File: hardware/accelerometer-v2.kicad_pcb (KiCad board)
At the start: 2 copper layers, 20 x 25 mm, 25 parts, among them P1 CON-SENSOR, P2 Debug, P3 Boot, U1 XMC1100, U2 KX122-1037, U3 DRILL, U4 DRILL, U5 DRILL, U6 DRILL

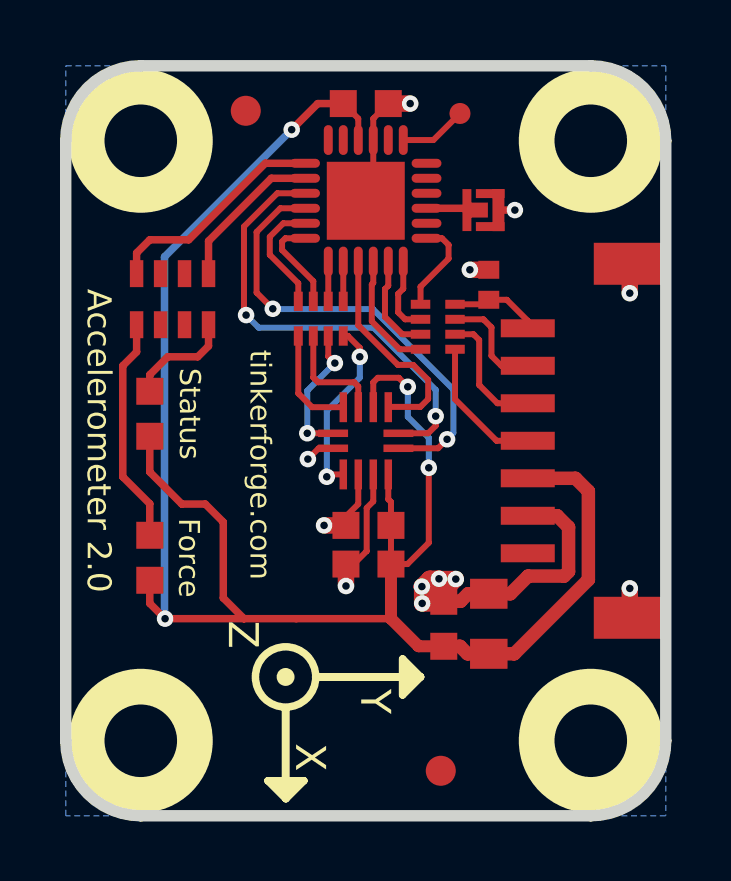
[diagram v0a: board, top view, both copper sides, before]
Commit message: fix footprint numbering and routing
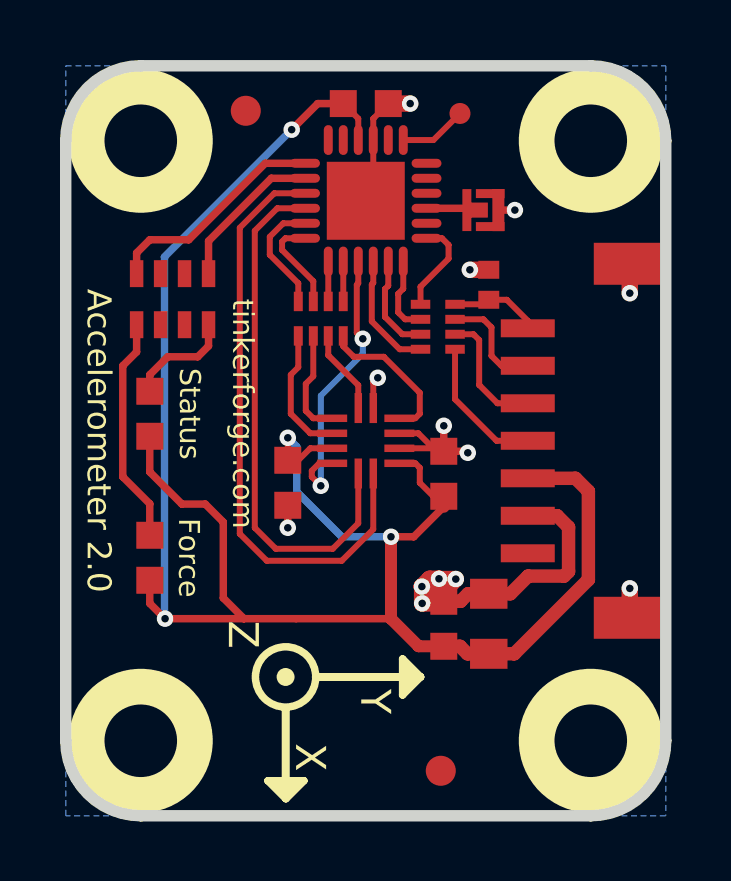
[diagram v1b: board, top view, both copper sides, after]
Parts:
- moved C5 3.82 mm to (128.9, 101.6), turned to 270 degrees
- moved C6 3.04 mm to (134.1, 101.3), turned to 90 degrees
- turned U2 to 0 degrees
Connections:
- P1 pad 1: Net-(P1-Pad1) -> (no net)
- RP2 pad 7: M-MOSI -> M-MISO
- RP2 pad 8: M-MISO -> M-MOSI
- RP3 pad 2: Net-(RP3-Pad2) -> (no net)
- RP3 pad 3: Net-(RP3-Pad3) -> (no net)
- RP3 pad 6: Net-(RP3-Pad6) -> (no net)
- RP3 pad 7: Net-(RP3-Pad7) -> (no net)
- U1 pad 11: Net-(U1-Pad11) -> (no net)
- U1 pad 12: Net-(U1-Pad12) -> (no net)
- U1 pad 15: INT1 -> INT2
- U1 pad 16: INT2 -> INT1
- U1 pad 17: M-MISO -> M-MOSI
- U1 pad 18: M-MOSI -> M-MISO
- U1 pad 2: Net-(U1-Pad2) -> (no net)
- U1 pad 4: Net-(U1-Pad4) -> (no net)
- U1 pad 5: Net-(U1-Pad5) -> (no net)
- U1 pad 6: Net-(U1-Pad6) -> (no net)
- U1 pad 8: Net-(U1-Pad8) -> (no net)
- U2 pad 1: Net-(RP2-Pad1) -> Net-(RP2-Pad2)
- U2 pad 2: Net-(RP2-Pad2) -> Net-(RP2-Pad1)
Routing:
- net INT2: track 15.4 -> 20.0 mm, vias 2 -> 0
- net TRIG: track 7.29 -> 9.57 mm, vias 0 -> 2
- net INT1: track 15.4 -> 17.6 mm, vias 2 -> 0
- net VCC: track 65.7 -> 67.7 mm
- net Net-(RP2-Pad3): track 4.58 -> 2.82 mm, vias 2 -> 0
- net GND: track 35.3 -> 34.2 mm, vias 12 -> 13
- net Net-(RP2-Pad4): track 6.05 -> 4.98 mm, vias 2 -> 0
- net Net-(RP2-Pad1): track 3.61 -> 4.35 mm
- net M-MOSI: track 3.24 -> 3.91 mm
- net M-MISO: track 3.91 -> 3.24 mm

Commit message: change processor xmc1100 -> xmc1302
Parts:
- U1: value XMC1100 -> XMC1302
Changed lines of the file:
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@@
-(kicad_pcb (version 20171130) (host pcbnew 5.0.1-33cea8e~67~ubuntu18.04.1)
+(kicad_pcb (version 20171130) (host pcbnew 5.0.1-33cea8e~68~ubuntu18.04.1)
   (general
     (thickness 1.6002)
@@
       (effects (font (size 0.3 0.3) (thickness 0.075)))
     )
-    (fp_text value XMC1100 (at 0 0.8 180) (layer F.Fab)
+    (fp_text value XMC1302 (at 0 0.8 180) (layer F.Fab)
       (effects (font (size 0.3 0.3) (thickness 0.075)))
     )
@@
   (segment (start 131.1 97.4) (end 132.1 97.4) (width 0.2) (layer Vorderseite) (net 17))
   (segment (start 130.7493 97.0493) (end 131.1 97.4) (width 0.2) (layer Vorderseite) (net 17))
+  (segment (start 129.475 92.95) (end 128.75 92.95) (width 0.2) (layer Vorderseite) (net 18))
+  (segment (start 129.2507 94.9507) (end 129.2507 95.555) (width 0.2) (layer Vorderseite) (net 18))
+  (segment (start 128.3 94) (end 129.2507 94.9507) (width 0.2) (layer Vorderseite) (net 18))
+  (segment (start 128.3 93.4) (end 128.3 94) (width 0.2) (layer Vorderseite) (net 18))
+  (segment (start 128.75 92.95) (end 128.3 93.4) (width 0.2) (layer Vorderseite) (net 18))
+  (segment (start 130.25 94.225) (end 130.25 95.55392) (width 0.2) (layer Vorderseite) (net 19))
+  (segment (start 130.25 95.55392) (end 130.24892 95.555) (width 0.2) (layer Vorderseite) (net 19))
+  (segment (start 130.75 94.225) (end 130.75 95.5543) (width 0.2) (layer Vorderseite) (net 20))
+  (segment (start 130.75 95.5543) (end 130.7493 95.555) (width 0.2) (layer Vorderseite) (net 20))
   (segment (start 129.475 93.45) (end 128.82 93.45) (width 0.2) (layer Vorderseite) (net 21))
   (segment (start 129.75108 94.88108) (end 129.75108 95.555) (width 0.2) (layer Vorderseite) (net 21))
@@
   (segment (start 128.71 93.56) (end 128.71 93.84) (width 0.2) (layer Vorderseite) (net 21))
   (segment (start 128.82 93.45) (end 128.71 93.56) (width 0.2) (layer Vorderseite) (net 21))
-  (segment (start 130.25 94.225) (end 130.25 95.55392) (width 0.2) (layer Vorderseite) (net 19))
-  (segment (start 130.25 95.55392) (end 130.24892 95.555) (width 0.2) (layer Vorderseite) (net 19))
-  (segment (start 130.75 94.225) (end 130.75 95.5543) (width 0.2) (layer Vorderseite) (net 20))
-  (segment (start 130.75 95.5543) (end 130.7493 95.555) (width 0.2) (layer Vorderseite) (net 20))
-  (segment (start 129.475 92.95) (end 128.75 92.95) (width 0.2) (layer Vorderseite) (net 18))
-  (segment (start 129.2507 94.9507) (end 129.2507 95.555) (width 0.2) (layer Vorderseite) (net 18))
-  (segment (start 128.3 94) (end 129.2507 94.9507) (width 0.2) (layer Vorderseite) (net 18))
-  (segment (start 128.3 93.4) (end 128.3 94) (width 0.2) (layer Vorderseite) (net 18))
-  (segment (start 128.75 92.95) (end 128.3 93.4) (width 0.2) (layer Vorderseite) (net 18))
   (segment (start 131.75 101.29) (end 131.75 103.15) (width 0.2) (layer Vorderseite) (net 22) (status 400000))
   (segment (start 128.45 91.95) (end 129.475 91.95) (width 0.2) (layer Vorderseite) (net 22) (status 800000))

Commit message: change back to xmc1100
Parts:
- U1: value XMC1302 -> XMC1100
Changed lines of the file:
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@@
       (effects (font (size 0.3 0.3) (thickness 0.075)))
     )
-    (fp_text value XMC1302 (at 0 0.8 180) (layer F.Fab)
+    (fp_text value XMC1100 (at 0 0.8 180) (layer F.Fab)
       (effects (font (size 0.3 0.3) (thickness 0.075)))
     )

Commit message: change force led to green
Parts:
- D2: value red -> green
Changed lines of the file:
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@@
       (effects (font (size 0.2 0.2) (thickness 0.05)))
     )
-    (fp_text value red (at 0.75 0.45 90) (layer F.Fab)
+    (fp_text value green (at 0.75 0.45 90) (layer F.Fab)
       (effects (font (size 0.2 0.2) (thickness 0.05)))
     )

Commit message: change processor to xmc1302
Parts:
- U1: value XMC1100 -> XMC1302
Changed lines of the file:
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@@
       (effects (font (size 0.3 0.3) (thickness 0.075)))
     )
-    (fp_text value XMC1100 (at 0 0.8 180) (layer F.Fab)
+    (fp_text value XMC1302 (at 0 0.8 180) (layer F.Fab)
       (effects (font (size 0.3 0.3) (thickness 0.075)))
     )
